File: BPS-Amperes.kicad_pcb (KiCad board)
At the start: 2 copper layers, 40 x 35 mm, 52 parts, among them J1 ShuntConn, J2 LeaderConn, J3 Conn_01x04, J4 Conn_01x05, U1 INA186A3IDDFT, U2 RO-123.3S_HP, U3 LTC6820, U4 HX1188FNL, U5 REF1930AIDDCT, U6 LTC2315, U7 OPA2196

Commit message: picket fence
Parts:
- J1, J4: moved to B.Cu
- moved C3 0.80 mm to (145.0, 106.8)
- moved C5 0.80 mm to (144.9, 108.8)
- moved D1 0.80 mm to (148.5, 106.8)
- moved R2 0.80 mm to (148.5, 108.8)
- moved R9 0.65 mm to (127.7, 106.0)
- turned J1 to 180 degrees
- turned J4 to 180 degrees
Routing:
- net +1V5: track 29.5 -> 34.8 mm, vias 2 -> 1
- net +3V0: track 53.6 -> 48.7 mm, vias 3 -> 4
- net Net-(C16-Pad1): track 11.7 -> 10.2 mm
- net GNDPWR: track 44.8 -> 45.6 mm
- net GND: track 49.1 -> 49.9 mm, vias 15 -> 41
- net +3V3: track 108.0 -> 108.8 mm
- net +12V: track 39.8 -> 40.6 mm

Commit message: text
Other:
- board text added: "Manthan approved this pull request. github.com/ manthanand"
- board text removed: "Hannah was here"
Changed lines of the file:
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@@
     (property "Sheetname" "")
     (attr smd)
-    (fp_text reference "U4" (at 7.5 0 90) (layer "F.SilkS")
+    (fp_text reference "U4" (at 7.5 0 90) (layer "F.SilkS") hide
       (effects (font (size 0.801614 0.801614) (thickness 0.05)))
     )
-    (fp_text value "HX1188FNL" (at -0.50895 1.50142) (layer "F.SilkS")
+    (fp_text value "HX1188FNL" (at -0.50895 1.50142) (layer "F.SilkS") hide
       (effects (font (size 0.641203 0.641203) (thickness 0.05)))
     )
@@
     (effects (font (size 0.8 0.8) (thickness 0.15)))
   )
-  (gr_text "Hannah\nwas\nhere" (at 141.5 118) (layer "F.SilkS")
+  (gr_text "Manthan approved\nthis pull request.\ngithub.com/\n	manthanand" (at 141.5 118) (layer "F.SilkS")
     (effects (font (size 0.8 0.8) (thickness 0.15)))
   )

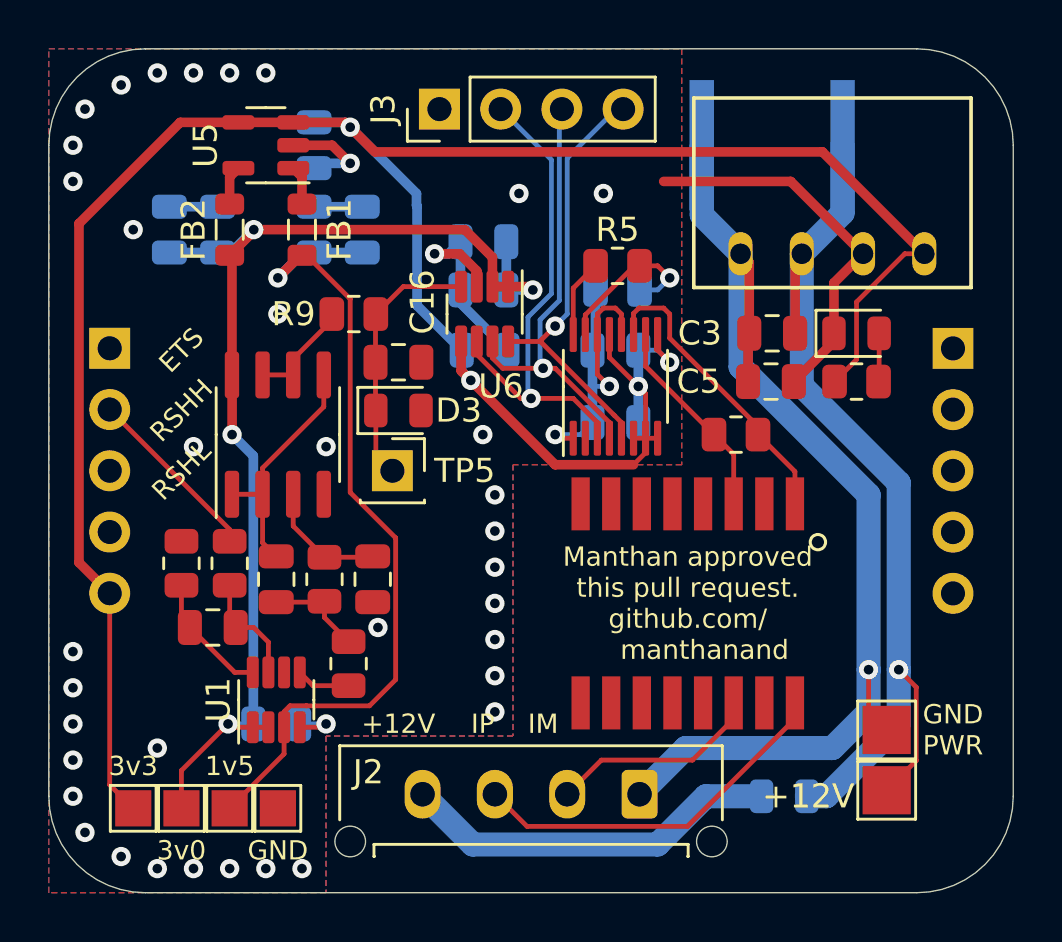
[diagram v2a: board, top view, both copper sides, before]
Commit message: Added silkscreens
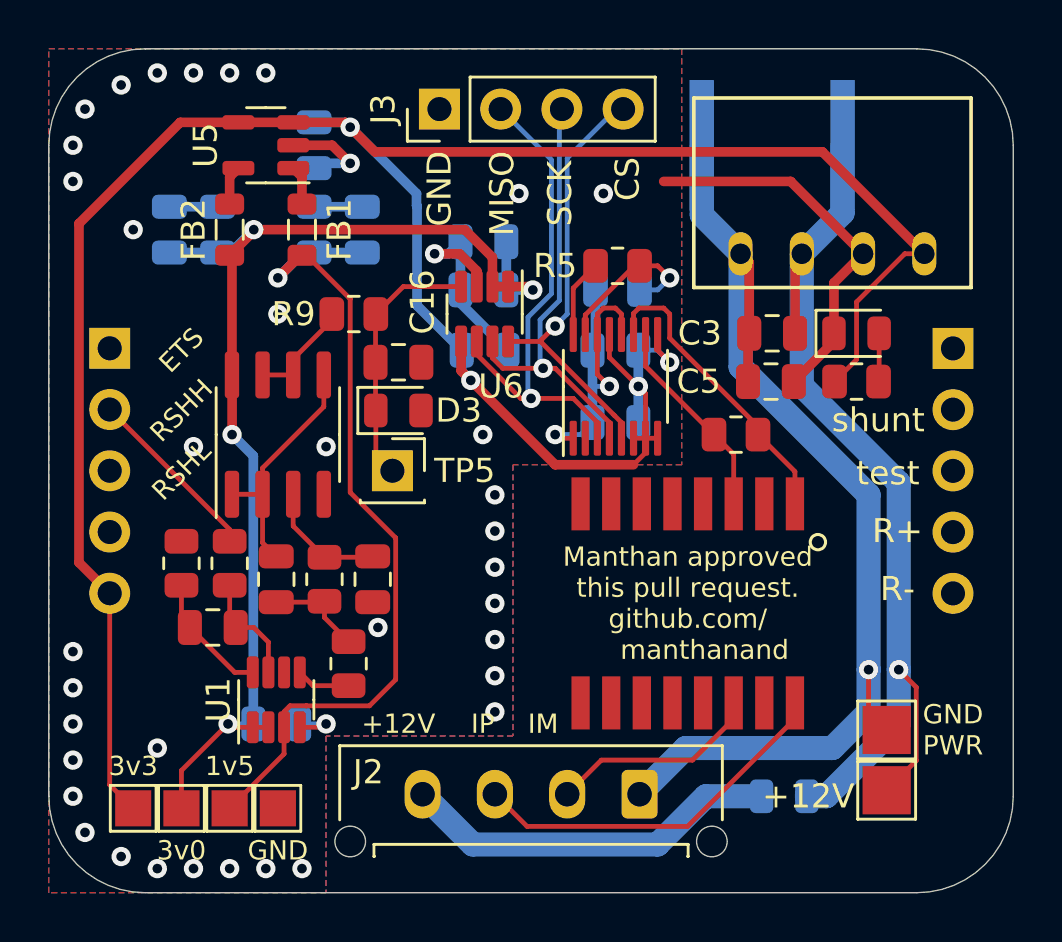
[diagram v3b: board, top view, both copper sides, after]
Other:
- board text added: "CS"
- board text added: "MISO"
- board text added: "R+"
- board text added: "R-"
- board text added: "SCK"
- board text added: "shunt"
- board text added: "test"
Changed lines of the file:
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@@
     (property "Sheetname" "")
     (attr smd)
-    (fp_text reference "R5" (at 0 1.5) (layer "F.SilkS")
+    (fp_text reference "R5" (at 2.5875 0) (layer "F.SilkS")
       (effects (font (size 1 1) (thickness 0.15)))
     )
@@
     (effects (font (size 1 1) (thickness 0.15)) (justify mirror))
   )
+  (gr_text "test" (at 149.8 112.6) (layer "F.SilkS")
+    (effects (font (size 1 1) (thickness 0.2)))
+  )
+  (gr_text "MISO" (at 133.8 101 90) (layer "F.SilkS")
+    (effects (font (size 1 1) (thickness 0.2)))
+  )
   (gr_text "3v3\n" (at 118.5 124.75) (layer "F.SilkS")
     (effects (font (size 0.8 0.8) (thickness 0.15)))
   )
+  (gr_text "CS" (at 139 100.4 90) (layer "F.SilkS")
+    (effects (font (size 1 1) (thickness 0.2)))
+  )
   (gr_text "+12V" (at 146.5 126) (layer "F.SilkS")
     (effects (font (size 1 1) (thickness 0.15)))
@@
     (effects (font (size 0.8 0.8) (thickness 0.15)))
   )
+  (gr_text "shunt\n" (at 149.4 110.4) (layer "F.SilkS")
+    (effects (font (size 1 1) (thickness 0.2)))
+  )
+  (gr_text "R-" (at 150.2 117.4) (layer "F.SilkS")
+    (effects (font (size 1 1) (thickness 0.2)))
+  )
   (gr_text "ETS" (at 120.5 107.5 45) (layer "F.SilkS")
     (effects (font (size 0.8 0.8) (thickness 0.15)))
@@
     (effects (font (size 0.8 0.8) (thickness 0.15)))
   )
+  (gr_text "GND" (at 131.2 100.8 90) (layer "F.SilkS")
+    (effects (font (size 1 1) (thickness 0.2)))
+  )
   (gr_text "IM" (at 135.5 123) (layer "F.SilkS")
     (effects (font (size 0.8 0.8) (thickness 0.15)))
@@
     (effects (font (size 0.8 0.8) (thickness 0.15)))
   )
+  (gr_text "SCK" (at 136.2 101 90) (layer "F.SilkS")
+    (effects (font (size 1 1) (thickness 0.2)))
+  )
+  (gr_text "R+" (at 150.2 115) (layer "F.SilkS")
+    (effects (font (size 1 1) (thickness 0.2)))
+  )
   (gr_text "+12V" (at 129.5 123) (layer "F.SilkS")

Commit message: gerbers 🐹 and drills 🪛
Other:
- rule pad_to_mask_clearance: 0.051 -> 0.05
- rule solder_mask_min_width: 0.25 -> 0.2
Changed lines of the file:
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@@
   )
   (setup
-    (pad_to_mask_clearance 0.051)
-    (solder_mask_min_width 0.25)
+    (stackup
+      (layer "F.SilkS" (type "Top Silk Screen"))
+      (layer "F.Paste" (type "Top Solder Paste"))
+      (layer "F.Mask" (type "Top Solder Mask") (thickness 0.01))
+      (layer "F.Cu" (type "copper") (thickness 0.035))
+      (layer "dielectric 1" (type "core") (thickness 1.51) (material "FR4") (epsilon_r 4.5) (loss_tangent 0.02))
+      (layer "B.Cu" (type "copper") (thickness 0.035))
+      (layer "B.Mask" (type "Bottom Solder Mask") (thickness 0.01))
+      (layer "B.Paste" (type "Bottom Solder Paste"))
+      (layer "B.SilkS" (type "Bottom Silk Screen"))
+      (copper_finish "None")
+      (dielectric_constraints no)
+    )
+    (pad_to_mask_clearance 0.05)
+    (solder_mask_min_width 0.2)
     (pcbplotparams
       (layerselection 0x00010fc_ffffffff)
@@
     (fp_line (start 1 0.625) (end -1 0.625) (layer "F.Fab") (width 0.1))
     (fp_line (start -1 -0.625) (end 1 -0.625) (layer "F.Fab") (width 0.1))
-    (pad "1" smd roundrect (at -0.9125 0 90) (size 1.025 1.4) (layers "F.Cu" "F.Paste" "F.Mask") (roundrect_rratio 0.243902)
+    (pad "1" smd roundrect (at -0.9125 0 90) (size 1.025 1.4) (layers "F.Cu" "F.Paste" "F.Mask") (roundrect_rratio 0.243902439)
       (net 20 "Net-(C15-Pad1)") (pintype "passive"))
-    (pad "2" smd roundrect (at 0.9125 0 90) (size 1.025 1.4) (layers "F.Cu" "F.Paste" "F.Mask") (roundrect_rratio 0.243902)
+    (pad "2" smd roundrect (at 0.9125 0 90) (size 1.025 1.4) (layers "F.Cu" "F.Paste" "F.Mask") (roundrect_rratio 0.243902439)
       (net 17 "Net-(C7-Pad1)") (pintype "passive"))
     (model "${KICAD6_3DMODEL_DIR}/Resistor_SMD.3dshapes/R_0805_2012Metric.wrl"
@@
     (fp_line (start 1 0.625) (end -1 0.625) (layer "F.Fab") (width 0.1))
     (fp_line (start -1 0.625) (end -1 -0.625) (layer "F.Fab") (width 0.1))
-    (pad "1" smd roundrect (at -0.9125 0 270) (size 1.025 1.4) (layers "F.Cu" "F.Paste" "F.Mask") (roundrect_rratio 0.243902)
+    (pad "1" smd roundrect (at -0.9125 0 270) (size 1.025 1.4) (layers "F.Cu" "F.Paste" "F.Mask") (roundrect_rratio 0.243902439)
       (net 20 "Net-(C15-Pad1)") (pintype "passive"))
-    (pad "2" smd roundrect (at 0.9125 0 270) (size 1.025 1.4) (layers "F.Cu" "F.Paste" "F.Mask") (roundrect_rratio 0.243902)
+    (pad "2" smd roundrect (at 0.9125 0 270) (size 1.025 1.4) (layers "F.Cu" "F.Paste" "F.Mask") (roundrect_rratio 0.243902439)
       (net 18 "Net-(R7-Pad2)") (pintype "passive"))
     (model "${KICAD6_3DMODEL_DIR}/Resistor_SMD.3dshapes/R_0805_2012Metric.wrl"
@@
     (fp_line (start 1 0.625) (end -1 0.625) (layer "F.Fab") (width 0.1))
     (fp_line (start -1 -0.625) (end 1 -0.625) (layer "F.Fab") (width 0.1))
-    (pad "1" smd roundrect (at -0.9125 0 180) (size 1.025 1.4) (layers "F.Cu" "F.Paste" "F.Mask") (roundrect_rratio 0.243902)
+    (pad "1" smd roundrect (at -0.9125 0 180) (size 1.025 1.4) (layers "F.Cu" "F.Paste" "F.Mask") (roundrect_rratio 0.243902439)
       (net 9 "/IP") (pintype "passive"))
-    (pad "2" smd roundrect (at 0.9125 0 180) (size 1.025 1.4) (layers "F.Cu" "F.Paste" "F.Mask") (roundrect_rratio 0.243902)
+    (pad "2" smd roundrect (at 0.9125 0 180) (size 1.025 1.4) (layers "F.Cu" "F.Paste" "F.Mask") (roundrect_rratio 0.243902439)
       (net 8 "/IM") (pintype "passive"))
     (model "${KICAD6_3DMODEL_DIR}/Resistor_SMD.3dshapes/R_0805_2012Metric.wrl"
@@
     (fp_line (start -1 -0.625) (end 1 -0.625) (layer "F.Fab") (width 0.1))
     (fp_line (start -1 0.625) (end -1 -0.625) (layer "F.Fab") (width 0.1))
-    (pad "1" smd roundrect (at -0.9125 0 90) (size 1.025 1.4) (layers "F.Cu" "F.Paste" "F.Mask") (roundrect_rratio 0.243902)
+    (pad "1" smd roundrect (at -0.9125 0 90) (size 1.025 1.4) (layers "F.Cu" "F.Paste" "F.Mask") (roundrect_rratio 0.243902439)
       (net 5 "/RSHH") (pintype "passive"))
-    (pad "2" smd roundrect (at 0.9125 0 90) (size 1.025 1.4) (layers "F.Cu" "F.Paste" "F.Mask") (roundrect_rratio 0.243902)
+    (pad "2" smd roundrect (at 0.9125 0 90) (size 1.025 1.4) (layers "F.Cu" "F.Paste" "F.Mask") (roundrect_rratio 0.243902439)
       (net 39 "Net-(J1-Pad2)") (pintype "passive"))
     (model "${KICAD6_3DMODEL_DIR}/Resistor_SMD.3dshapes/R_0805_2012Metric.wrl"
@@
     (pad "" np_thru_hole circle (at -3 -1.96 180) (size 1.27 1.27) (drill 1.27) (layers *.Cu *.Mask))
     (pad "" np_thru_hole circle (at 12 -1.96 180) (size 1.27 1.27) (drill 1.27) (layers *.Cu *.Mask))
-    (pad "1" thru_hole roundrect (at 0 0 180) (size 1.5 2.02) (drill 1.02) (layers *.Cu *.Mask) (roundrect_rratio 0.166667)
+    (pad "1" thru_hole roundrect (at 0 0 180) (size 1.5 2.02) (drill 1.02) (layers *.Cu *.Mask) (roundrect_rratio 0.1666673333)
       (net 1 "GNDPWR") (pinfunction "Pin_1") (pintype "passive"))
     (pad "2" thru_hole oval (at 3 0 180) (size 1.5 2.02) (drill 1.02) (layers *.Cu *.Mask)
@@
     (fp_line (start -1 0.625) (end -1 -0.625) (layer "F.Fab") (width 0.1))
     (fp_line (start 1 0.625) (end -1 0.625) (layer "F.Fab") (width 0.1))
-    (pad "1" smd roundrect (at -0.9125 0 180) (size 1.025 1.4) (layers "F.Cu" "F.Paste" "F.Mask") (roundrect_rratio 0.243902)
+    (pad "1" smd roundrect (at -0.9125 0 180) (size 1.025 1.4) (layers "F.Cu" "F.Paste" "F.Mask") (roundrect_rratio 0.243902439)
       (net 11 "Net-(R5-Pad1)") (pintype "passive"))
-    (pad "2" smd roundrect (at 0.9125 0 180) (size 1.025 1.4) (layers "F.Cu" "F.Paste" "F.Mask") (roundrect_rratio 0.243902)
+    (pad "2" smd roundrect (at 0.9125 0 180) (size 1.025 1.4) (layers "F.Cu" "F.Paste" "F.Mask") (roundrect_rratio 0.243902439)
       (net 10 "Net-(R5-Pad2)") (pintype "passive"))
     (model "${KICAD6_3DMODEL_DIR}/Resistor_SMD.3dshapes/R_0805_2012Metric.wrl"
@@
     (fp_line (start -1 0.625) (end -1 -0.625) (layer "F.Fab") (width 0.1))
     (fp_line (start -1 -0.625) (end 1 -0.625) (layer "F.Fab") (width 0.1))
-    (pad "1" smd roundrect (at -0.9125 0 90) (size 1.025 1.4) (layers "F.Cu" "F.Paste" "F.Mask") (roundrect_rratio 0.243902)
+    (pad "1" smd roundrect (at -0.9125 0 90) (size 1.025 1.4) (layers "F.Cu" "F.Paste" "F.Mask") (roundrect_rratio 0.243902439)
       (net 21 "/RSHL") (pintype "passive"))
-    (pad "2" smd roundrect (at 0.9125 0 90) (size 1.025 1.4) (layers "F.Cu" "F.Paste" "F.Mask") (roundrect_rratio 0.243902)
+    (pad "2" smd roundrect (at 0.9125 0 90) (size 1.025 1.4) (layers "F.Cu" "F.Paste" "F.Mask") (roundrect_rratio 0.243902439)
       (net 3 "GND") (pintype "passive"))
     (model "${KICAD6_3DMODEL_DIR}/Resistor_SMD.3dshapes/R_0805_2012Metric.wrl"
@@
     (fp_line (start -1 -0.625) (end 1 -0.625) (layer "F.Fab") (width 0.1))
     (fp_line (start 1 0.625) (end -1 0.625) (layer "F.Fab") (width 0.1))
-    (pad "1" smd roundrect (at -0.9125 0) (size 1.025 1.4) (layers "F.Cu" "F.Paste" "F.Mask") (roundrect_rratio 0.243902)
+    (pad "1" smd roundrect (at -0.9125 0) (size 1.025 1.4) (layers "F.Cu" "F.Paste" "F.Mask") (roundrect_rratio 0.243902439)
       (net 4 "+3V3") (pintype "passive"))
-    (pad "2" smd roundrect (at 0.9125 0) (size 1.025 1.4) (layers "F.Cu" "F.Paste" "F.Mask") (roundrect_rratio 0.243902)
+    (pad "2" smd roundrect (at 0.9125 0) (size 1.025 1.4) (layers "F.Cu" "F.Paste" "F.Mask") (roundrect_rratio 0.243902439)
       (net 35 "Net-(D1-Pad2)") (pintype "passive"))
     (model "${KICAD6_3DMODEL_DIR}/Resistor_SMD.3dshapes/R_0805_2012Metric.wrl"
@@
     (fp_line (start 1 -0.625) (end 1 0.625) (layer "F.Fab") (width 0.1))
     (fp_line (start -1 0.625) (end -1 -0.625) (layer "F.Fab") (width 0.1))
-    (pad "1" smd roundrect (at -0.9125 0) (size 1.025 1.4) (layers "F.Cu" "F.Paste" "F.Mask") (roundrect_rratio 0.243902)
+    (pad "1" smd roundrect (at -0.9125 0) (size 1.025 1.4) (layers "F.Cu" "F.Paste" "F.Mask") (roundrect_rratio 0.243902439)
       (net 23 "Net-(R9-Pad1)") (pintype "passive"))
-    (pad "2" smd roundrect (at 0.9125 0) (size 1.025 1.4) (layers "F.Cu" "F.Paste" "F.Mask") (roundrect_rratio 0.243902)
+    (pad "2" smd roundrect (at 0.9125 0) (size 1.025 1.4) (layers "F.Cu" "F.Paste" "F.Mask") (roundrect_rratio 0.243902439)
       (net 22 "Net-(C16-Pad1)") (pintype "passive"))
     (model "${KICAD6_3DMODEL_DIR}/Resistor_SMD.3dshapes/R_0805_2012Metric.wrl"
@@
     (fp_line (start 1 -0.625) (end -1 -0.625) (layer "B.Fab") (width 0.1))
     (fp_line (start -1 0.625) (end 1 0.625) (layer "B.Fab") (width 0.1))
-    (pad "1" smd roundrect (at -0.9125 0) (size 1.025 1.4) (layers "B.Cu" "B.Paste" "B.Mask") (roundrect_rratio 0.243902)
+    (pad "1" smd roundrect (at -0.9125 0) (size 1.025 1.4) (layers "B.Cu" "B.Paste" "B.Mask") (roundrect_rratio 0.243902439)
       (net 3 "GND") (pintype "passive"))
-    (pad "2" smd roundrect (at 0.9125 0) (size 1.025 1.4) (layers "B.Cu" "B.Paste" "B.Mask") (roundrect_rratio 0.243902)
+    (pad "2" smd roundrect (at 0.9125 0) (size 1.025 1.4) (layers "B.Cu" "B.Paste" "B.Mask") (roundrect_rratio 0.243902439)
       (net 11 "Net-(R5-Pad1)") (pintype "passive"))
     (model "${KICAD6_3DMODEL_DIR}/Resistor_SMD.3dshapes/R_0805_2012Metric.wrl"
